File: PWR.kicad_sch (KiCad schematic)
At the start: 36 parts, among them J1 Conn_01x04_Pin, J10 Conn_01x02_Pin, J2 Conn_01x03_Pin, J3 Conn_01x03_Pin, J4 Conn_01x03_Pin, J5 Conn_01x03_Pin, U1 LM66100DCK, U2 XC6206P332MR, U4 MCP6001-OT

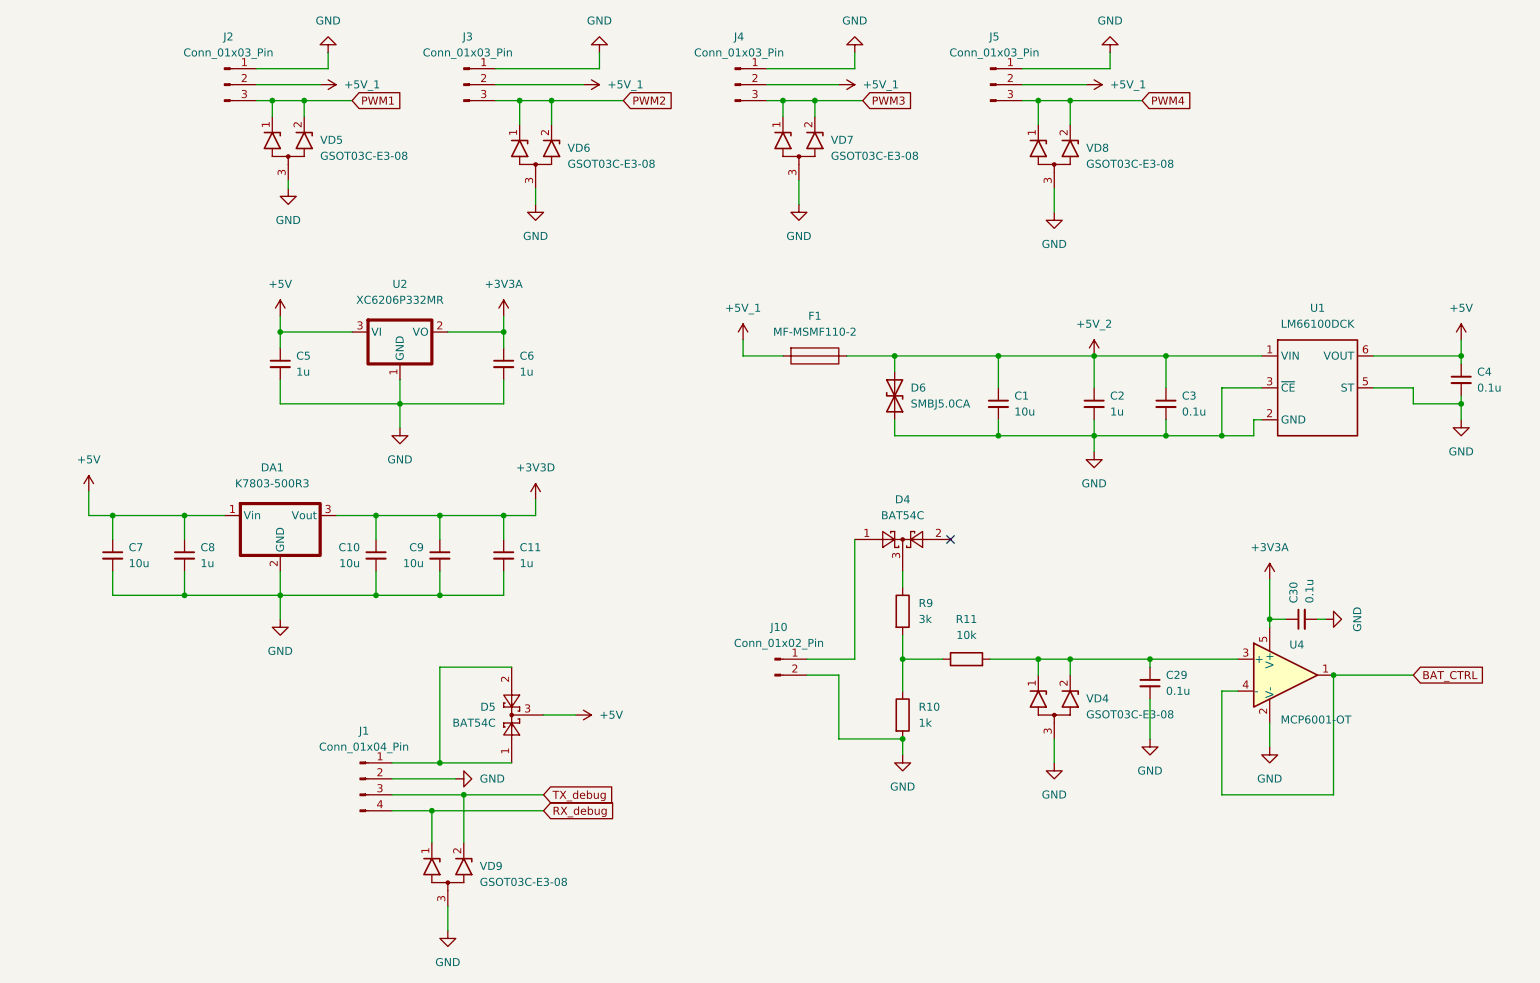
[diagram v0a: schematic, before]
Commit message: feat: добавлен вход питания, кроме dc-dc
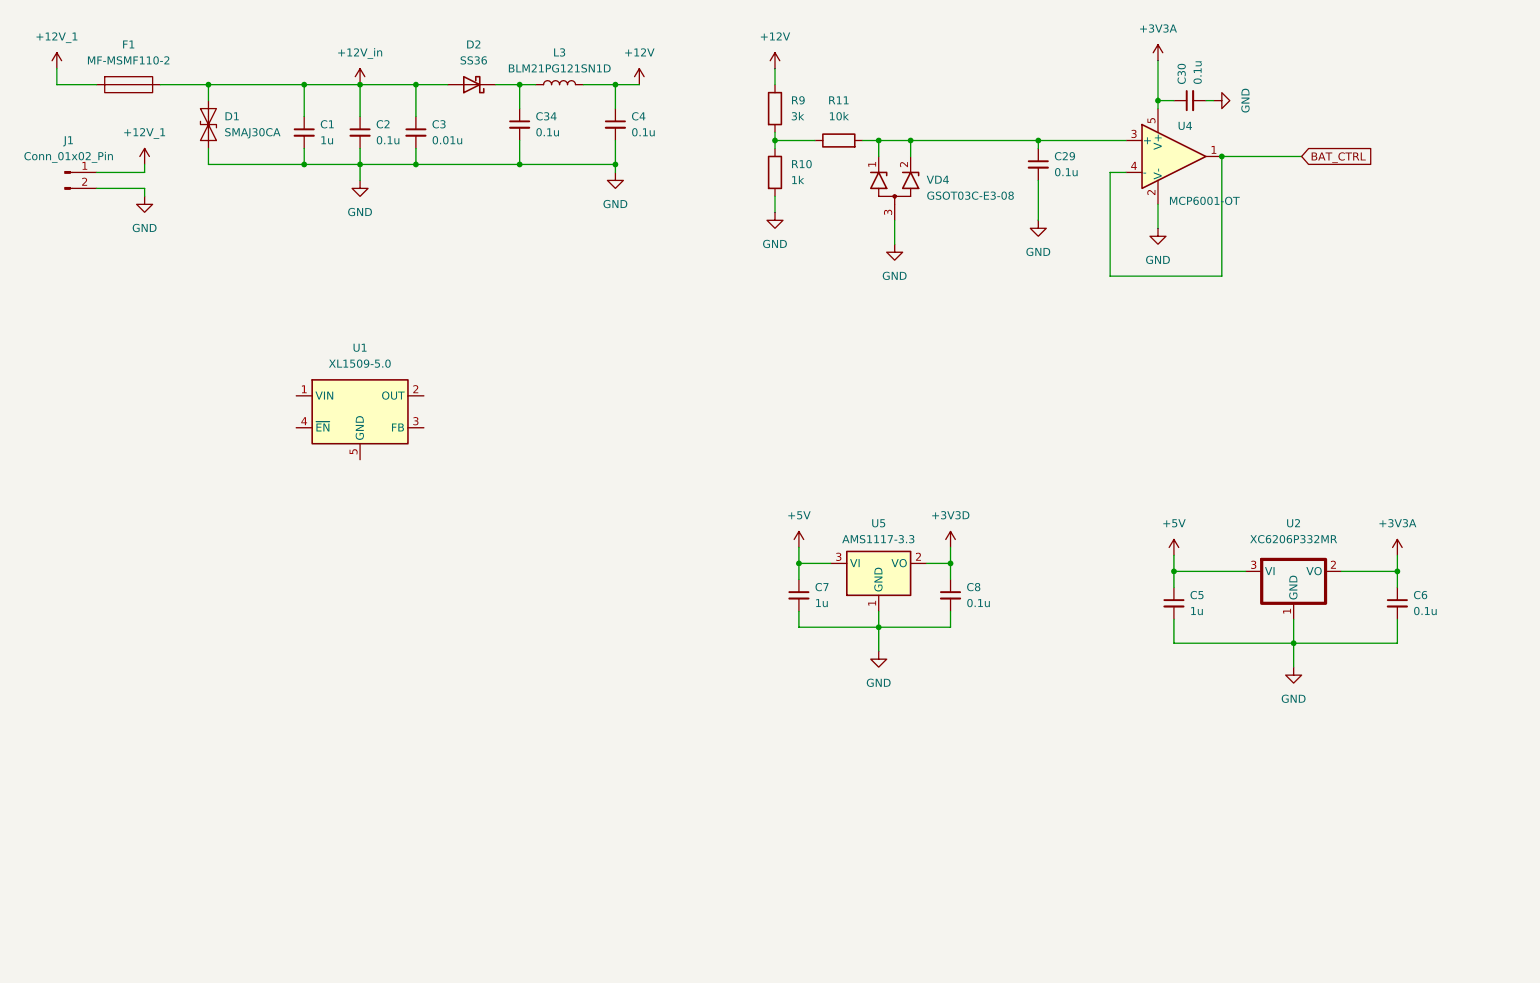
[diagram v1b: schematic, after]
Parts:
- removed C10, C9: 10u, Capacitor_SMD:C_0805_2012Metric_Pad1.18x1.45mm_HandSolder, symbol Device:C_Small
- removed C11: 1u, Capacitor_SMD:C_0805_2012Metric_Pad1.18x1.45mm_HandSolder, symbol Device:C_Small
- removed D4, D5: BAT54C, Package_TO_SOT_SMD:SOT-23_Handsoldering, symbol Diode:BAT54C
- removed D6: SMBJ5.0CA, Diode_SMD:D_SMB_Handsoldering, symbol TVS:SMBJ5.0CA
- removed DA1: K7803-500R3, Package_SIP:SIP3_11.6x8.5mm, symbol Power_suply:K7803-500R3
- removed J1: Conn_01x04_Pin, Connector_PinSocket_2.54mm:PinSocket_1x04_P2.54mm_Vertical, symbol Connector:Conn_01x04_Pin
- removed J10: Conn_01x02_Pin, Connector_Hirose:Hirose_DF13-02P-1.25DSA_1x02_P1.25mm_Vertical, symbol Connector:Conn_01x02_Pin
- removed J2, J3, J4, J5: Conn_01x03_Pin, Connector_PinHeader_2.54mm:PinHeader_1x03_P2.54mm_Horizontal, symbol Connector:Conn_01x03_Pin
- removed U1: LM66100DCK, Package_TO_SOT_SMD:SOT-363_SC-70-6, symbol Power_suply:LM66100DCK
- removed VD5, VD6, VD7, VD8, VD9: GSOT03C-E3-08, Package_TO_SOT_SMD:SOT-23_Handsoldering, symbol TWS:GSOT03C-E3-08
- added C34: 0.1u, Capacitor_SMD:C_0805_2012Metric_Pad1.18x1.45mm_HandSolder, symbol Device:C_Small
- added D1: SMAJ30CA, Diode_SMD:D_SMA, symbol Diode:SMAJ30CA
- added D2: SS36, Diode_SMD:D_SMA, symbol Diode:SS36
- added J1: Conn_01x02_Pin, Connector_PinHeader_2.54mm:PinHeader_1x02_P2.54mm_Vertical, symbol Connector:Conn_01x02_Pin
- added L3: BLM21PG121SN1D, Inductor_SMD:L_0805_2012Metric_Pad1.05x1.20mm_HandSolder, symbol Inductors:L
- added U1: XL1509-5.0, Package_SO:SOIC-8_3.9x4.9mm_P1.27mm, symbol Regulator_Switching:XL1509-5.0
- added U5: AMS1117-3.3, Package_TO_SOT_SMD:SOT-223-3_TabPin2, symbol Regulator_Linear:AMS1117-3.3
- C1, C7: value 10u -> 1u
- C2, C6, C8: value 1u -> 0.1u
- C3: value 0.1u -> 0.01u
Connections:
- net +3V3D: now also C8.1, U5.2 (VO)
- net +5V: now also U5.3 (VI); no longer C4.1, C8.1
- net GND: now also C34.2, D1.1 (A1), J1.2 (Pin_2), U5.1 (GND)
- net +12V: now reaches R9.1
- net +12V: now also C4.1, L3.2
- net +5V_1 renamed +12V_1
- net +12V_1: now also J1.1 (Pin_1)
- net +5V_2 renamed +12V_in
- net +12V_in: now also D1.2 (A2), D2.2 (A)
- new net: C34.1, D2.1 (K), L3.1
- new net: U1.5 (GND), U1.6 (GND), U1.7 (GND), U1.8 (GND)
- no-connect marks 1 -> 0
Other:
- moved on the sheet: C1, C2, C29, C3, C30, C4, C5, C6, F1, R10, R11, R9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

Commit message: feat: доработана схема питания, расчечены габариты печатной платы
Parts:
- removed U1: XL1509-5.0, Package_SO:SOIC-8_3.9x4.9mm_P1.27mm, symbol Regulator_Switching:XL1509-5.0
- added C10, C11: 100u, Capacitor_SMD:C_Elec_6.3x7.7, symbol Device:C_Small_US
- added C43, C44, C9: 0.1u, Capacitor_SMD:C_0805_2012Metric_Pad1.18x1.45mm_HandSolder, symbol Device:C_Small
- added D3: SS36, Diode_SMD:D_SMA, symbol Diode:SS36
- added L4: 47uH, Inductor_SMD:L_12x12mm_H8mm, symbol Inductors:L
- added L5: BLM21PG121SN1D, Inductor_SMD:L_0805_2012Metric_Pad1.05x1.20mm_HandSolder, symbol Inductors:L
- added U6: XL1509-5.0, Package_SO:SOIC-8_3.9x4.9mm_P1.27mm, symbol Power_suply:XL1509-5.0
- C1: value 1u -> 0.01u
- C3: value 0.01u -> 1u
- C5, C7: value 1u -> 0.1u
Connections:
- net +12V: now also C11.1, C44.1, U6.1 (VIN)
- net +5V: now also C9.1, L5.2
- net GND: now also C10.2, C11.2, C43.2, C44.2, C9.2, D3.2 (A), U6.4 (~{EN}), U6.5 (GND), U6.6 (GND), U6.7 (GND), U6.8 (GND)
- new net: C10.1, C43.1, L4.2, L5.1, U6.3 (FB)
- new net: D3.1 (K), L4.1, U6.2 (OUT)
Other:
- moved on the sheet: C1, C2, C29, C3, C30, C34, C4, C5, C6, C7, C8, D1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

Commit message: feat: Добавил внешние интерфейсы
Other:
- moved on the sheet: C29
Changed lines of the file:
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@@
 	)
 	(junction
-		(at 191.77 68.58)
-		(diameter 0)
-		(color 0 0 0 0)
-	)
-	(junction
 		(at 64.77 119.38)
 		(diameter 0)
@@
 	)
 	(junction
+		(at 191.77 68.58)
+		(diameter 0)
+		(color 0 0 0 0)
+	)
+	(junction
 		(at 78.74 115.57)
 		(diameter 0)
@@
 	(wire
 		(pts
-			(xy 191.77 74.93) (xy 191.77 81.28)
+			(xy 191.77 78.74) (xy 191.77 81.28)
 		)
 		(stroke
@@
 	(wire
 		(pts
-			(xy 191.77 68.58) (xy 191.77 69.85)
+			(xy 191.77 68.58) (xy 191.77 73.66)
 		)
 		(stroke
@@
 	(symbol
 		(lib_id "Device:C_Small")
-		(at 191.77 72.39 0)
+		(at 191.77 76.2 0)
 		(unit 1)
 		(body_style 1)
@@
 		(fields_autoplaced yes)
 		(property "Reference" "C29"
-			(at 194.31 71.1262 0)
+			(at 194.31 74.9362 0)
 			(show_name no)
 			(do_not_autoplace no)
@@
 		)
 		(property "Value" "0.1u"
-			(at 194.31 73.6662 0)
+			(at 194.31 77.4762 0)
 			(show_name no)
 			(do_not_autoplace no)
@@
 		)
 		(property "Footprint" "Capacitor_SMD:C_0805_2012Metric_Pad1.18x1.45mm_HandSolder"
-			(at 191.77 72.39 0)
+			(at 191.77 76.2 0)
 			(hide yes)
 			(show_name no)
@@
 		)
 		(property "Datasheet" ""
-			(at 191.77 72.39 0)
+			(at 191.77 76.2 0)
 			(hide yes)
 			(show_name no)
@@
 		)
 		(property "Description" "Unpolarized capacitor, small symbol"
-			(at 191.77 72.39 0)
+			(at 191.77 76.2 0)
 			(hide yes)
 			(show_name no)
